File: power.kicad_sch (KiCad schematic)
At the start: 6 parts, among them J2 Conn_01x02_Pin, U4 LM7805_TO220

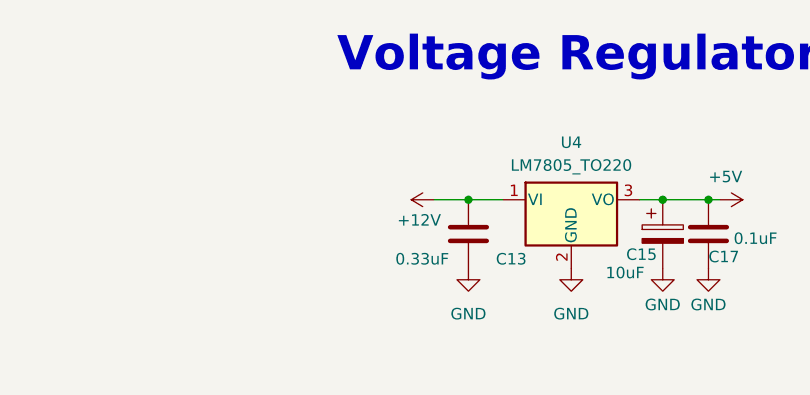
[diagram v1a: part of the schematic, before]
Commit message: Switched the diodes on the fan to Schottkys and added a Schottky to input of power regulator
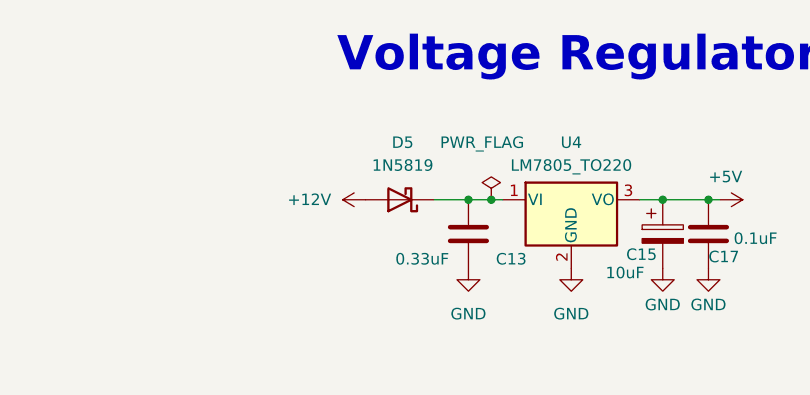
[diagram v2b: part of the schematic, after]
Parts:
- added D5: 1N5819, Diode_THT:D_DO-41_SOD81_P10.16mm_Horizontal, symbol Diode:1N5819
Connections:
- net +12V: now also D5.2 (A); no longer C13.2, U4.1 (VI)
- new net: C13.2, D5.1 (K), U4.1 (VI)
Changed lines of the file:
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@@
+	)
+	(junction
+		(at 152.4 69.85)
+		(diameter 0)
+		(color 0 0 0 0)
 	)
 	(junction
@@
 	(wire
 		(pts
-			(xy 149.86 69.85) (xy 153.67 69.85)
+			(xy 152.4 69.85) (xy 153.67 69.85)
+		)
+		(stroke
+			(width 0)
+			(type default)
+		)
+	)
+	(wire
+		(pts
+			(xy 149.86 69.85) (xy 152.4 69.85)
 		)
 		(stroke
@@
 	)
 	(symbol
+		(lib_id "Diode:1N5819")
+		(at 142.24 69.85 180)
+		(unit 1)
+		(body_style 1)
+		(exclude_from_sim no)
+		(in_bom yes)
+		(on_board yes)
+		(in_pos_files yes)
+		(dnp no)
+		(fields_autoplaced yes)
+		(property "Reference" "D5"
+			(at 142.5575 63.5 0)
+			(show_name no)
+			(do_not_autoplace no)
+			(effects
+				(font
+					(size 1.27 1.27)
+				)
+			)
+		)
+		(property "Value" "1N5819"
+			(at 142.5575 66.04 0)
+			(show_name no)
+			(do_not_autoplace no)
+			(effects
+				(font
+					(size 1.27 1.27)
+				)
+			)
+		)
+		(property "Footprint" "Diode_THT:D_DO-41_SOD81_P10.16mm_Horizontal"
+			(at 142.24 65.405 0)
+			(hide yes)
+			(show_name no)
+			(do_not_autoplace no)
+			(effects
+				(font
+					(size 1.27 1.27)
+				)
+			)
+		)
+		(property "Datasheet" "http://www.vishay.com/docs/88525/1n5817.pdf"
+			(at 142.24 69.85 0)
+			(hide yes)
+			(show_name no)
+			(do_not_autoplace no)
+			(effects
+				(font
+					(size 1.27 1.27)
+				)
+			)
+		)
+		(property "Description" "40V 1A Schottky Barrier Rectifier Diode, DO-41"
+			(at 142.24 69.85 0)
+			(hide yes)
+			(show_name no)
+			(do_not_autoplace no)
+			(effects
+				(font
+					(size 1.27 1.27)
+				)
+			)
+		)
+		(pin "1"
+		)
+		(pin "2"
+		)
+		(instances
+			(project "Actual_Indonesia_PCB"
+				(path "/47496e5c-34fd-4328-9694-83983cdb3752/05b1c396-c7b9-4a28-944a-b7c865229a2e"
+					(reference "D5")
+					(unit 1)
+				)
+			)
+		)
+	)
+	(symbol
 		(lib_id "power:GND")
 		(at 149.86 77.47 0)
@@
 	)
 	(symbol
+		(lib_id "power:PWR_FLAG")
+		(at 152.4 69.85 0)
+		(unit 1)
+		(body_style 1)
+		(exclude_from_sim no)
+		(in_bom yes)
+		(on_board yes)
+		(in_pos_files yes)
+		(dnp no)
+		(property "Reference" "#FLG02"
+			(at 152.4 67.945 0)
+			(hide yes)
+			(show_name no)
+			(do_not_autoplace no)
+			(effects
+				(font
+					(size 1.27 1.27)
+				)
+			)
+		)
+		(property "Value" "PWR_FLAG"
+			(at 151.384 63.5 0)
+			(show_name no)
+			(do_not_autoplace no)
+			(effects
+				(font
+					(size 1.27 1.27)
+				)
+			)
+		)
+		(property "Footprint" ""
+			(at 152.4 69.85 0)
+			(hide yes)
+			(show_name no)
+			(do_not_autoplace no)
+			(effects
+				(font
+					(size 1.27 1.27)
+				)
+			)
+		)
+		(property "Datasheet" ""
+			(at 152.4 69.85 0)
+			(hide yes)
+			(show_name no)
+			(do_not_autoplace no)
+			(effects
+				(font
+					(size 1.27 1.27)
+				)
+			)
+		)
+		(property "Description" "Special symbol for telling ERC where power comes from"
+			(at 152.4 69.85 0)
+			(hide yes)
+			(show_name no)
+			(do_not_autoplace no)
+			(effects
+				(font
+					(size 1.27 1.27)
+				)
+			)
+		)
+		(pin "1"
+		)
+		(instances
+			(project "Actual_Indonesia_PCB"
+				(path "/47496e5c-34fd-4328-9694-83983cdb3752/05b1c396-c7b9-4a28-944a-b7c865229a2e"
+					(reference "#FLG02")
+					(unit 1)
+				)
+			)
+		)
+	)
+	(symbol
 		(lib_id "Regulator_Linear:LM7805_TO220")
 		(at 161.29 69.85 0)
@@
 	)
 	(symbol
-		(lib_id "power:+12V")
-		(at 146.05 69.85 90)
-		(unit 1)
-		(body_style 1)
-		(exclude_from_sim no)
-		(in_bom yes)
-		(on_board yes)
-		(in_pos_files yes)
-		(dnp no)
-		(property "Reference" "#PWR0115"
-			(at 149.86 69.85 0)
-			(hide yes)
-			(show_name no)
-			(do_not_autoplace no)
-			(effects
-				(font
-					(size 1.27 1.27)
-				)
-			)
-		)
-		(property "Value" "+12V"
-			(at 146.812 72.136 90)
-			(show_name no)
-			(do_not_autoplace no)
-			(effects
-				(font
-					(size 1.27 1.27)
-				)
-				(justify left)
-			)
-		)
-		(property "Footprint" ""
-			(at 146.05 69.85 0)
-			(hide yes)
-			(show_name no)
-			(do_not_autoplace no)
-			(effects
-				(font
-					(size 1.27 1.27)
-				)
-			)
-		)
-		(property "Datasheet" ""
-			(at 146.05 69.85 0)
-			(hide yes)
-			(show_name no)
-			(do_not_autoplace no)
-			(effects
-				(font
-					(size 1.27 1.27)
-				)
-			)
-		)
-		(property "Description" "Power symbol creates a global label with name \"+12V\""
-			(at 146.05 69.85 0)
-			(hide yes)
-			(show_name no)
-			(do_not_autoplace no)
-			(effects
-				(font
-					(size 1.27 1.27)
-				)
-			)
-		)
-		(pin "1"
-		)
-		(instances
-			(project "Actual_Indonesia_PCB"
-				(path "/47496e5c-34fd-4328-9694-83983cdb3752/05b1c396-c7b9-4a28-944a-b7c865229a2e"
-					(reference "#PWR0115")
-					(unit 1)
-				)
-			)
-		)
-	)
-	(symbol
 		(lib_id "power:GND")
 		(at 161.29 77.47 0)
@@
 					(unit 1)
 				)
+			)
+		)
+	)
+	(symbol
+		(lib_id "power:+12V")
+		(at 138.43 69.85 90)
+		(unit 1)
+		(body_style 1)
+		(exclude_from_sim no)
+		(in_bom yes)
+		(on_board yes)
+		(in_pos_files yes)
+		(dnp no)
+		(fields_autoplaced yes)
+		(property "Reference" "#PWR07"
+			(at 142.24 69.85 0)
+			(hide yes)
+			(show_name no)
+			(do_not_autoplace no)
+			(effects
+				(font
+					(size 1.27 1.27)
+				)
+			)
+		)
+		(property "Value" "+12V"
+			(at 134.62 69.8499 90)
+			(show_name no)
+			(do_not_autoplace no)
+			(effects
+				(font
+					(size 1.27 1.27)
+				)
+				(justify left)
+			)
+		)
+		(property "Footprint" ""
+			(at 138.43 69.85 0)
+			(hide yes)
+			(show_name no)
+			(do_not_autoplace no)
+			(effects
+				(font
+					(size 1.27 1.27)
+				)
+			)
+		)
+		(property "Datasheet" ""
+			(at 138.43 69.85 0)
+			(hide yes)
+			(show_name no)
+			(do_not_autoplace no)
+			(effects
+				(font
+					(size 1.27 1.27)
+				)
+			)
+		)
+		(property "Description" "Power symbol creates a global label with name \"+12V\""
+			(at 138.43 69.85 0)
+			(hide yes)
+			(show_name no)
+			(do_not_autoplace no)
+			(effects
+				(font
+					(size 1.27 1.27)
+				)
+			)
+		)
+		(pin "1"
+		)
+		(instances
+			(project "Actual_Indonesia_PCB"
+				(path "/47496e5c-34fd-4328-9694-83983cdb3752/05b1c396-c7b9-4a28-944a-b7c865229a2e"
+					(reference "#PWR07")
+					(unit 1)
+				)

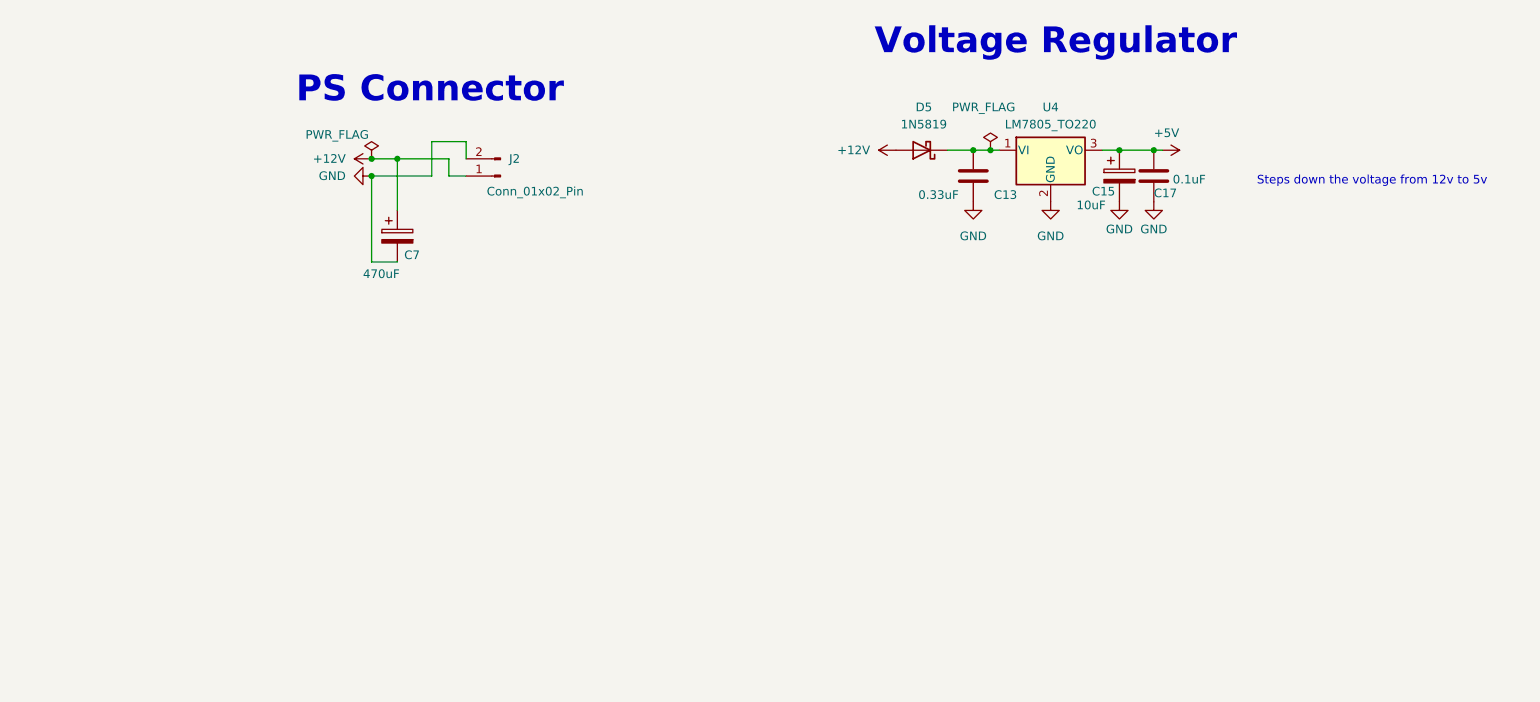
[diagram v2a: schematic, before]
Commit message: Fixed Schottky orientation, created 3 individual 12V pwr lines, fixed Schottky/resistor placement on layout
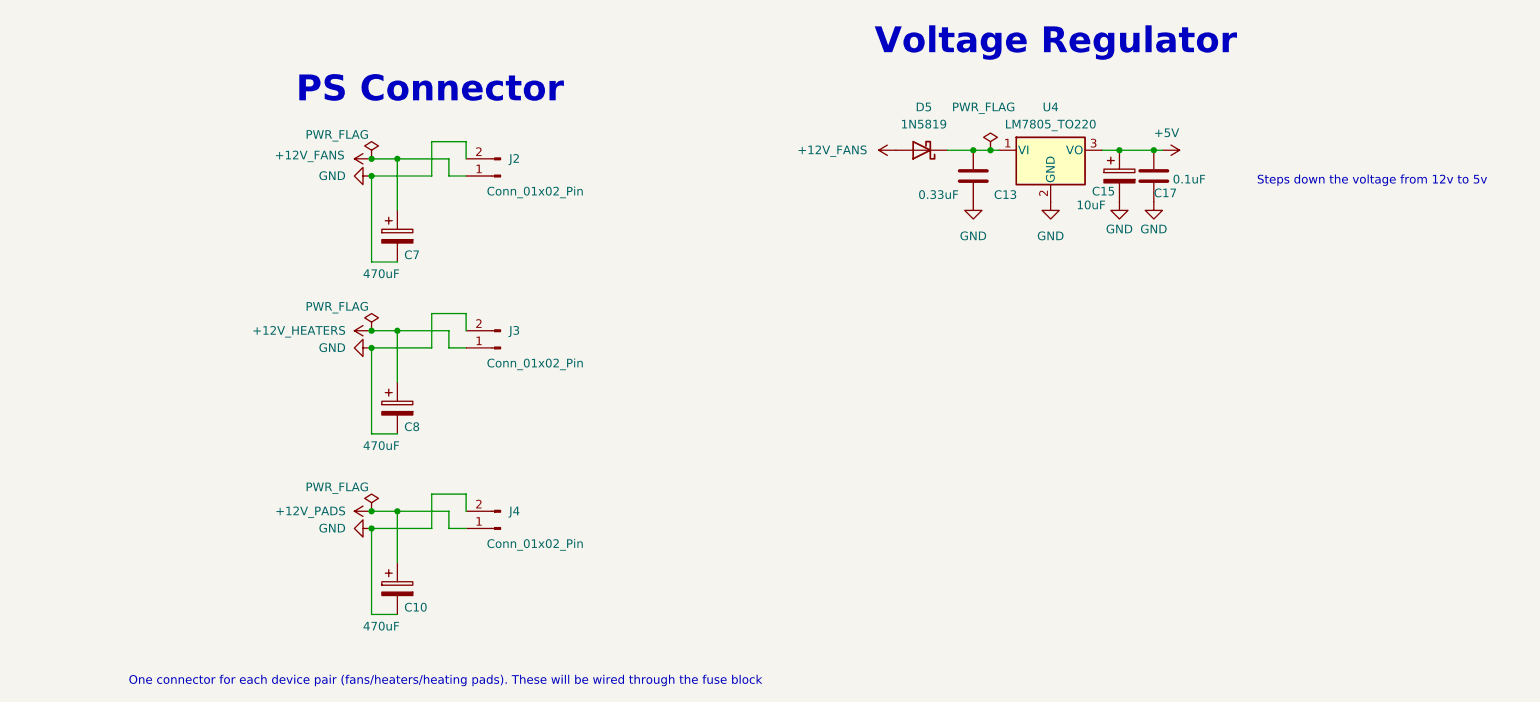
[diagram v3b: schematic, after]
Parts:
- added C10, C8: 470uF, Capacitor_THT:CP_Radial_D10.0mm_P5.00mm, symbol Device:C_Polarized
- added J3, J4: Conn_01x02_Pin, Connector_AMASS:AMASS_XT60-M_1x02_P7.20mm_Vertical, symbol Connector:Conn_01x02_Pin
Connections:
- net GND: now also C10.2, C8.2, J3.2 (Pin_2), J4.2 (Pin_2)
- net +12V renamed +12V_FANS
- new net +12V_HEATERS: C8.1, J3.1 (Pin_1)
- new net +12V_PADS: C10.1, J4.1 (Pin_1)
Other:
- note added: "One connector for each device pair (fans/heaters/heating pads). These will be wired through the fuse block"
